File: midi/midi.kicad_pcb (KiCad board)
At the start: 2 copper layers, 69.8 x 125.1 mm, 50 parts, among them J1 Conn_01x02, J2 SJ-43515TS-SMT-TR, M1 DMG4466SSS-13, U1 ESP32-S3-WROOM-1-n16, U2 LTC1624CS8_TRPBF, U3 MAX98357A, U4 MAX98357A, U5 CD74HC154M96

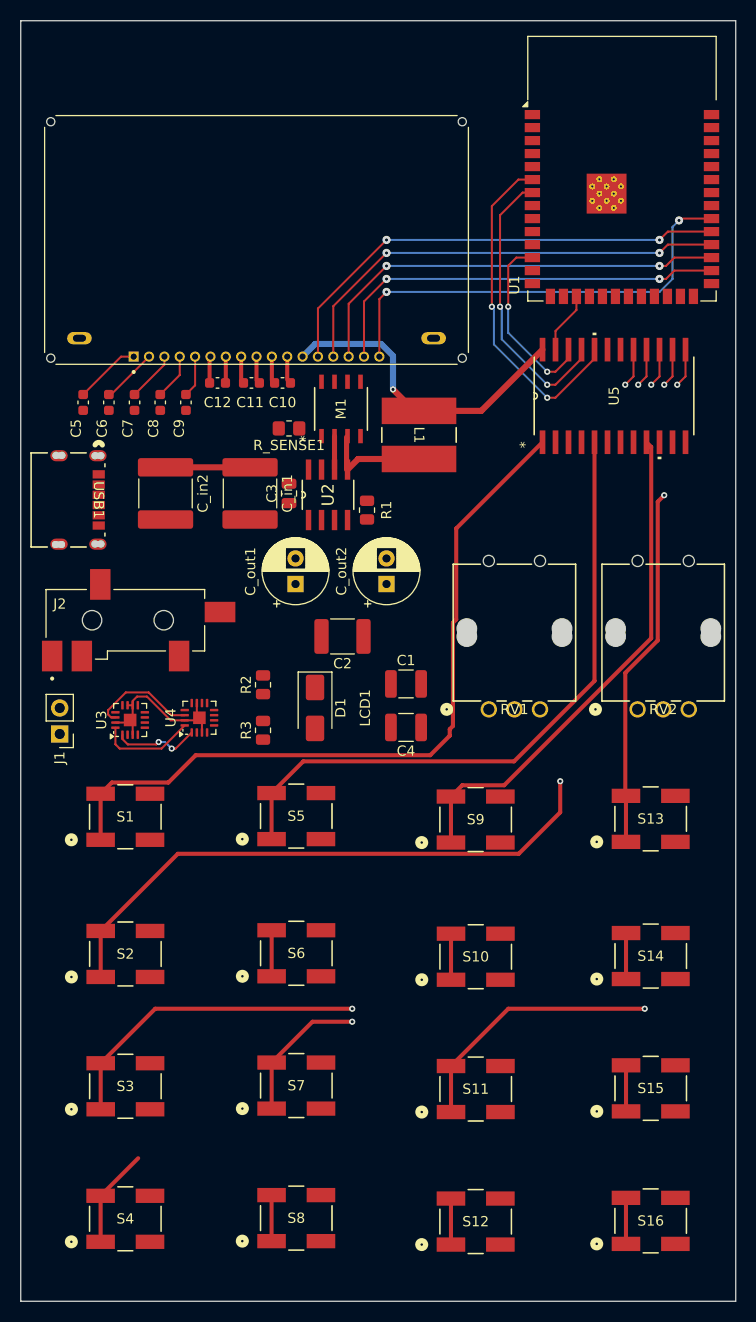
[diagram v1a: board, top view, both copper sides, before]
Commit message: assign more footprints
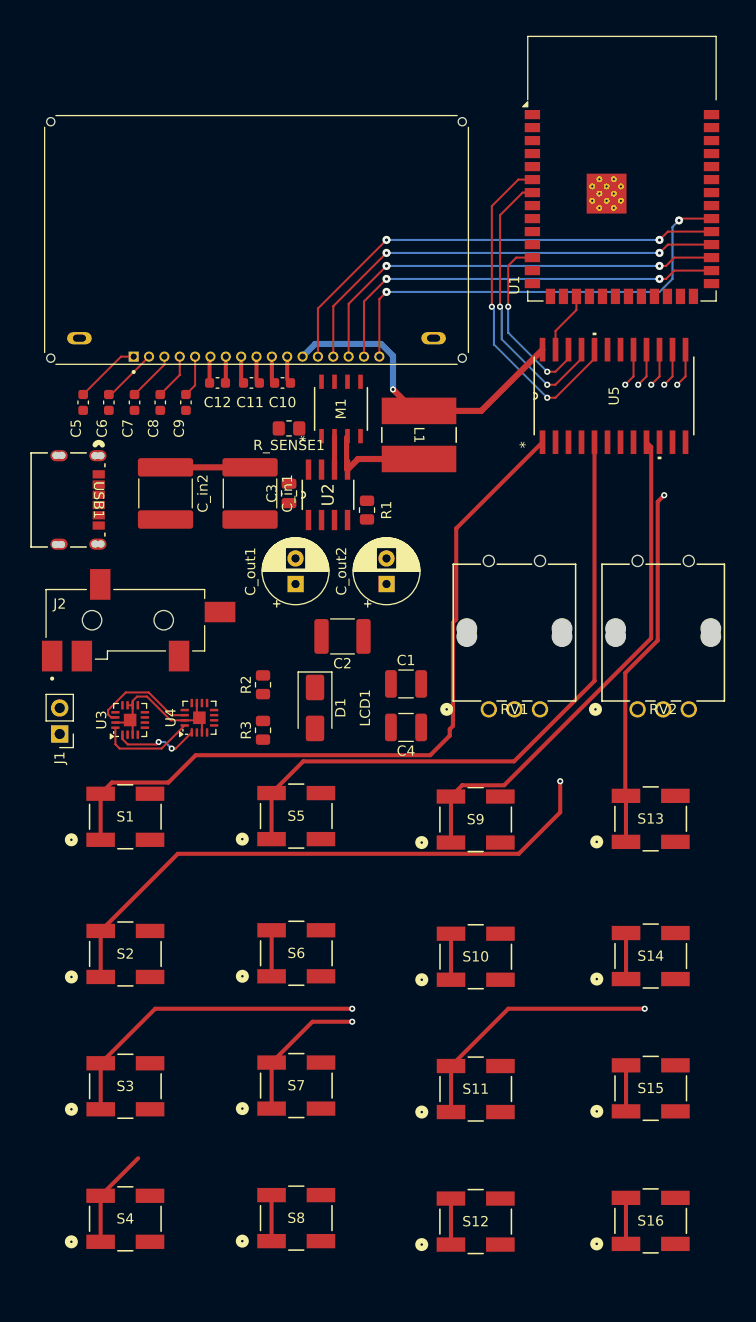
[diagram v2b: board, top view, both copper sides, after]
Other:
- board size 69.8 x 125.1 mm -> 4.4 x 8.7 mm
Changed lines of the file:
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@@
 		)
-	)
-	(gr_line
-		(start 119.38 39.37)
-		(end 119.38 164.465)
-		(stroke
-			(width 0.05)
-			(type default)
-		)
-		(layer "Edge.Cuts")
-	)
-	(gr_line
-		(start 49.53 164.465)
-		(end 49.53 39.37)
-		(stroke
-			(width 0.05)
-			(type default)
-		)
-		(layer "Edge.Cuts")
-	)
-	(gr_line
-		(start 49.53 39.37)
-		(end 119.38 39.37)
-		(stroke
-			(width 0.05)
-			(type default)
-		)
-		(layer "Edge.Cuts")
-	)
-	(gr_line
-		(start 119.38 164.465)
-		(end 49.53 164.465)
-		(stroke
-			(width 0.05)
-			(type default)
-		)
-		(layer "Edge.Cuts")
 	)
 	(segment

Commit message: layout progress
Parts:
- removed C_in1, C_in2: 22µF / 35V, Capacitor_SMD:C_2220_5750Metric
- removed C_out1, C_out2: 100µF / 10V, Capacitor_THT:CP_Radial_D6.3mm_P2.50mm
- removed D1: MBRS340T3, Diode_SMD:D_SMA
- removed M1: DMG4466SSS-13, DMG4466SSS_13:SO-8_DIO
- removed R_SENSE1: 0.05Ω, Resistor_SMD:R_0805_2012Metric_Pad1.20x1.40mm_HandSolder
- removed S1, S10, S11, S12, S13, S14, S15, S16, S2, S3, S4, S5, S6, S7, S8, S9: KS-01Q-01_Obsolete, BTN_TL3301AF160QJ:TL3301AF160QJ_EWI
- removed USB1: USB4125-GF-A, USB4125_GF_A:CONN6_USB4125_GCT
- added C13: .1µF, Capacitor_SMD:C_0603_1608Metric_Pad1.08x0.95mm_HandSolder, F.Cu at (164.5, 71.8)
- added C14: .1µF, Capacitor_SMD:C_0603_1608Metric_Pad1.08x0.95mm_HandSolder, F.Cu at (164.5, 75.6)
- added J3: USB_C_Receptacle_USB2.0_16P, USB4105-GF-A:GCT_USB4105-GF-A, F.Cu at (213.4, 82.5)
- added R4: 5.1k, Resistor_SMD:R_0805_2012Metric_Pad1.20x1.40mm_HandSolder, F.Cu at (210.2, 92.7)
- added R5: 5.1k, Resistor_SMD:R_0805_2012Metric_Pad1.20x1.40mm_HandSolder, F.Cu at (210.2, 97.2)
- added SW1: Reset, Button_Switch_THT:SW_PUSH_6mm_H5mm, F.Cu at (176.0, 69.6)
- added SW10: SW_Push, Button_Switch_THT:SW_PUSH_6mm_H5mm, F.Cu at (208.2, 150.2)
- added SW11: SW_Push, Button_Switch_THT:SW_PUSH_6mm_H5mm, F.Cu at (152.4, 104.4)
- added SW12: SW_Push, Button_Switch_THT:SW_PUSH_6mm_H5mm, F.Cu at (152.4, 119.0)
- added SW13: SW_Push, Button_Switch_THT:SW_PUSH_6mm_H5mm, F.Cu at (170.7, 104.5)
- added SW14: SW_Push, Button_Switch_THT:SW_PUSH_6mm_H5mm, F.Cu at (189.8, 104.5)
- added SW15: SW_Push, Button_Switch_THT:SW_PUSH_6mm_H5mm, F.Cu at (208.1, 104.5)
- added SW16: SW_Push, Button_Switch_THT:SW_PUSH_6mm_H5mm, F.Cu at (170.7, 119.0)
- added SW17: SW_Push, Button_Switch_THT:SW_PUSH_6mm_H5mm, F.Cu at (189.8, 119.0)
- added SW18: SW_Push, Button_Switch_THT:SW_PUSH_6mm_H5mm, F.Cu at (208.2, 119.0)
- added SW2: Boot, Button_Switch_THT:SW_PUSH_6mm_H5mm, F.Cu at (151.8, 65.4)
- added SW3: SW_Push, Button_Switch_THT:SW_PUSH_6mm_H5mm, F.Cu at (152.4, 134.3)
- added SW4: SW_Push, Button_Switch_THT:SW_PUSH_6mm_H5mm, F.Cu at (170.7, 134.3)
- added SW5: SW_Push, Button_Switch_THT:SW_PUSH_6mm_H5mm, F.Cu at (189.8, 134.3)
- added SW6: SW_Push, Button_Switch_THT:SW_PUSH_6mm_H5mm, F.Cu at (208.2, 134.3)
- added SW7: SW_Push, Button_Switch_THT:SW_PUSH_6mm_H5mm, F.Cu at (152.4, 149.9)
- added SW8: SW_Push, Button_Switch_THT:SW_PUSH_6mm_H5mm, F.Cu at (170.7, 150.2)
- added SW9: SW_Push, Button_Switch_THT:SW_PUSH_6mm_H5mm, F.Cu at (189.7, 150.2)
- C1: value 100pF -> 22µF; footprint Capacitor_SMD:C_1210_3225Metric -> Capacitor_SMD:C_0603_1608Metric_Pad1.08x0.95mm_HandSolder
- C2: value 470pF -> 10µF; footprint Capacitor_SMD:C_1812_4532Metric -> Capacitor_SMD:C_0603_1608Metric_Pad1.08x0.95mm_HandSolder
- C3: value 1000pF -> .1µF; footprint Capacitor_SMD:C_0805_2012Metric -> Capacitor_SMD:C_0603_1608Metric_Pad1.08x0.95mm_HandSolder
- C4: value 0.1µ -> 1µF; footprint Capacitor_SMD:C_1210_3225Metric -> Capacitor_SMD:C_0603_1608Metric_Pad1.08x0.95mm_HandSolder
- L1: value 10µH -> 1µH; footprint SRR6038_100Y:IND_BOURNS_SRR6038 -> Inductor_SMD:L_0805_2012Metric_Pad1.15x1.40mm_HandSolder
- R1: value 6.8k -> 634k; footprint Resistor_SMD:R_0805_2012Metric -> Resistor_SMD:R_0603_1608Metric_Pad0.98x0.95mm_HandSolder
- R2: value 35.7k -> 634k; footprint Resistor_SMD:R_0805_2012Metric -> Resistor_SMD:R_0603_1608Metric_Pad0.98x0.95mm_HandSolder
- R3: value 20k -> 10k; footprint Resistor_SMD:R_0805_2012Metric -> Resistor_SMD:R_0603_1608Metric_Pad0.98x0.95mm_HandSolder
- U1: value ESP32-S3-WROOM-1-n16 -> ESP32-S2-SOLO; footprint RF_Module:ESP32-S3-WROOM-1 -> PCM_Espressif:ESP32-S2-SOLO
- U2: value LTC1624CS8_TRPBF -> SC189ZSKTRT; footprint LTC1624CS8_TRPBF:SOIC127P600X175-8N -> SC189ZSKTRT:SOT23-5-SC189_SEM
- moved J2 165.8 mm to (214.7, 67.0), turned to 180 degrees
- moved J1 154.0 mm to (204.5, 79.4), turned to 0 degrees
- moved C2 133.4 mm to (214.0, 89.9), turned to -90 degrees
- moved R3 132.4 mm to (204.5, 91.4), turned to 180 degrees
- moved U4 131.2 mm to (192.9, 70.5), turned to 0 degrees
- moved U3 129.1 mm to (183.8, 70.5), turned to 0 degrees
- moved C10 126.2 mm to (200.7, 61.6)
- moved U2 125.7 mm to (204.8, 96.5)
- moved C11 125.5 mm to (196.8, 61.6)
- moved C12 125.1 mm to (193.2, 61.6)
- moved C6 125.0 mm to (182.3, 62.2)
- moved C9 125.0 mm to (189.9, 62.2)
- moved C5 125.0 mm to (179.8, 62.2)
- moved C7 125.0 mm to (184.8, 62.2)
- moved C8 125.0 mm to (187.4, 62.2)
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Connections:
- C1 pad 1: Net-(U2-VFB) -> +3V3
- C1 pad 2: Net-(U2-GND) -> GND
- C2 pad 1: Net-(C2-Pad1) -> +5V
- C2 pad 2: Net-(U2-ITH/RUN) -> GND
- C3 pad 1: Net-(U2-SENSE-) -> GND
- C3 pad 2: /5V -> Net-(U1-EN)
- C4 pad 1: Net-(U2-BOOST) -> GND
- C4 pad 2: Net-(D1-K) -> +3V3
- L1 pad 1: Net-(D1-K) -> Net-(U2-LX)
- L1 pad 2: /3V3 -> +3V3
- LCD1 pad 12: /3V3 -> +3V3
- R1 pad 1: Net-(U2-GND) -> +3V3
- R1 pad 2: Net-(C2-Pad1) -> Net-(U3-~{SD_MODE})
- R2 pad 1: Net-(U2-VFB) -> +3V3
- R2 pad 2: /3V3 -> Net-(U4-~{SD_MODE})
- R3 pad 1: GND -> +3V3
- R3 pad 2: Net-(U2-VFB) -> Net-(U1-EN)
- U1 pad 11: unconnected-(U1-IO18-Pad11) -> /AUDIO.BCLK
- U1 pad 12: /BTND1 -> unconnected-(U1-GPIO8/TOUCH8/ADC1_CH7-Pad12)
- U1 pad 13: unconnected-(U1-IO19-Pad13) -> /USB.D-
- U1 pad 14: unconnected-(U1-IO20-Pad14) -> /USB.D+
- U1 pad 15: unconnected-(U1-IO3-Pad15) -> /AUDIO.DIN
- U1 pad 16: /AUDIO.DIN -> unconnected-(U1-GPIO46-Pad16)
- U1 pad 17: /BTND0 -> unconnected-(U1-GPIO9/TOUCH9/ADC1_CH8/FSPIHD-Pad17)
- U1 pad 2: /3V3 -> +3V3
- U1 pad 23: unconnected-(U1-IO21-Pad23) -> /LCD.RST
- U1 pad 24: /AUDIO.BCLK -> unconnected-(U1-SPIIO4/GPIO33/FSPIHD-Pad24)
- U1 pad 25: /AUDIO.LRCLK -> /LCD.CS1
- U1 pad 26: /S18 -> /LCD.A0
- U1 pad 27: unconnected-(U1-IO0-Pad27) -> Net-(U1-GPIO0)
- U1 pad 28: /LCD.RST -> /LCD.SI
- U1 pad 29: /LCD.A0 -> /LCD.SCL
- U1 pad 3: /EN-ESP32 -> Net-(U1-EN)
- U1 pad 30: /LCD.SCL -> unconnected-(U1-SPIDQS/GPIO37/FSPIQ-Pad30)
- U1 pad 31: /LCD.SI -> unconnected-(U1-GPIO38/FSPIWP-Pad31)
- U1 pad 32: /LCD.CS1 -> /BTND0
- U1 pad 33: unconnected-(U1-IO40-Pad33) -> /BTND1
- U1 pad 34: unconnected-(U1-IO41-Pad34) -> /BTND2
- U1 pad 35: /S17 -> /BTND3
- U1 pad 38: unconnected-(U1-IO2-Pad38) -> /RV2
- U1 pad 39: unconnected-(U1-IO1-Pad39) -> /RV1
- U1 pad 4: /RV1 -> /AUDIO.LRCLK
- U1 pad 5: /RV2 -> unconnected-(U1-GPIO5/TOUCH5/ADC1_CH4-Pad5)
- U1 pad 6: /BTND3 -> unconnected-(U1-GPIO6/TOUCH6/ADC1_CH5-Pad6)
- U1 pad 7: /BTND2 -> unconnected-(U1-GPIO7/TOUCH7/ADC1_CH6-Pad7)
- U2 pad 1: Net-(U2-SENSE-) -> +5V
- U2 pad 2: Net-(U2-ITH/RUN) -> GND
- U2 pad 3: Net-(U2-VFB) -> +5V
- U2 pad 4: Net-(U2-GND) -> +3V3
- U2 pad 5: Net-(D1-K) -> Net-(U2-LX)
- U3 pad 2: unconnected-(U3-GAIN_SLOT-Pad2) -> +3V3
- U3 pad 4: unconnected-(U3-~{SD_MODE}-Pad4) -> Net-(U3-~{SD_MODE})
- U3 pad 7: /3V3 -> +3V3
- U3 pad 8: /3V3 -> +3V3
- U4 pad 2: unconnected-(U4-GAIN_SLOT-Pad2) -> +3V3
- U4 pad 4: unconnected-(U4-~{SD_MODE}-Pad4) -> Net-(U4-~{SD_MODE})
- U4 pad 7: /3V3 -> +3V3
- U4 pad 8: /3V3 -> +3V3
- U5 pad 24: /3V3 -> +3V3
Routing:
- net +3V3: track 0.00 -> 151.2 mm, vias 0 -> 7
- net /RV2: track 0.00 -> 118.3 mm
- net /RV1: track 0.00 -> 94.6 mm
- net Net-(U1-EN): track 0.00 -> 89.9 mm, vias 0 -> 2
- net /USB.D-: track 0.00 -> 74.8 mm, vias 0 -> 2
- net /USB.D+: track 0.00 -> 72.9 mm, vias 0 -> 2
- net /S6: track 4.50 -> 76.4 mm, vias 0 -> 1
- net /S8: track 4.50 -> 70.9 mm, vias 0 -> 1
- net /S4: track 9.69 -> 74.9 mm, vias 0 -> 3
- net /S7: track 14.0 -> 68.8 mm, vias 1 -> 3
- net /S10: track 4.50 -> 57.7 mm, vias 0 -> 3
- net /AUDIO.LRCLK: track 10.4 -> 58.2 mm, vias 0 -> 3
- net /S15: track 8.26 -> 54.7 mm, vias 1 -> 2
- net /AUDIO.BCLK: track 9.50 -> 54.0 mm, vias 0 -> 3
- net /S14: track 8.26 -> 51.7 mm, vias 1 -> 2
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- added copper zone on B.Cu, net GND
- added copper zone on F.Cu, net GND
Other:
- board size 4.4 x 8.7 mm -> 73 x 129.5 mm

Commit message: fix some layout issues
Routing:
- net Net-(U1-GPIO0): track 24.4 -> 37.4 mm
- net GND: track 17.1 -> 28.3 mm, vias 2 -> 4
- net Net-(U1-EN): track 89.9 -> 94.8 mm
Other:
- board size 73 x 129.5 mm -> 74.9 x 129.5 mm

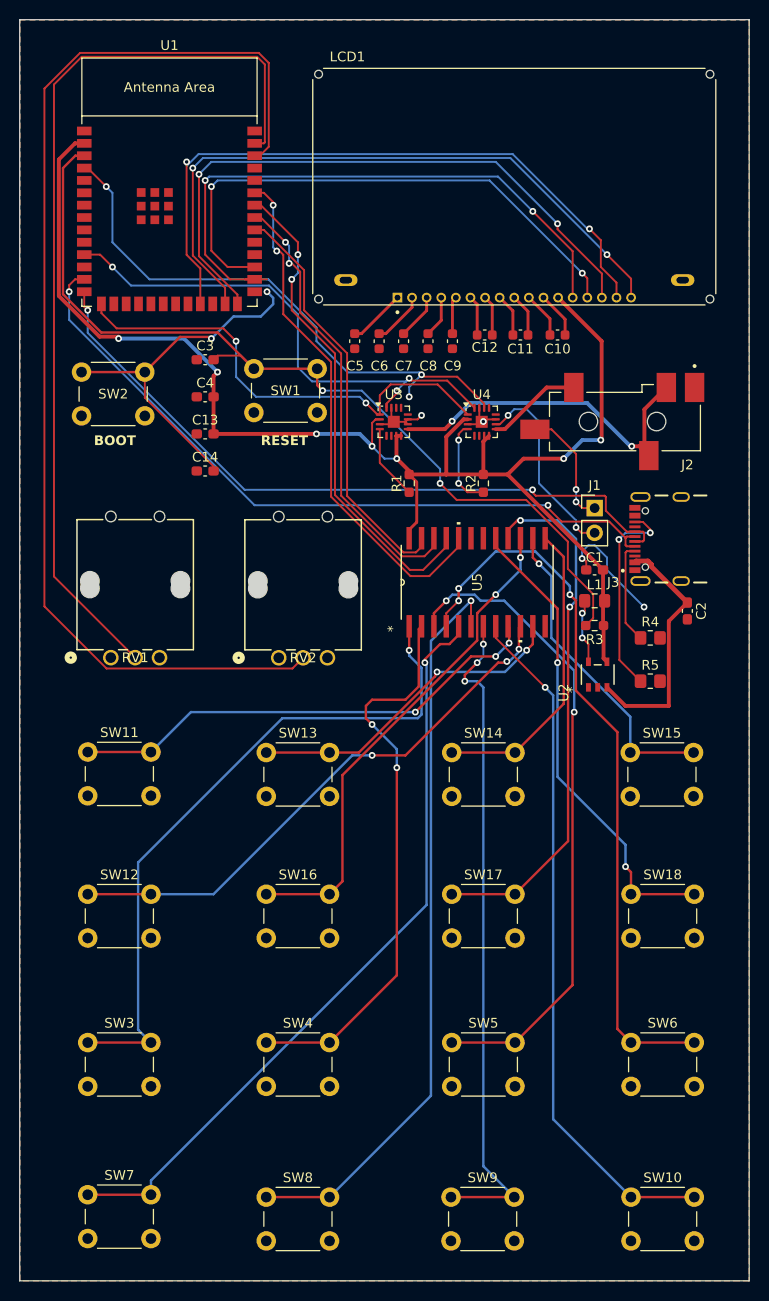
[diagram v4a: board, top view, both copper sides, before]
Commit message: fixed ~60 clearance errors around LCD area
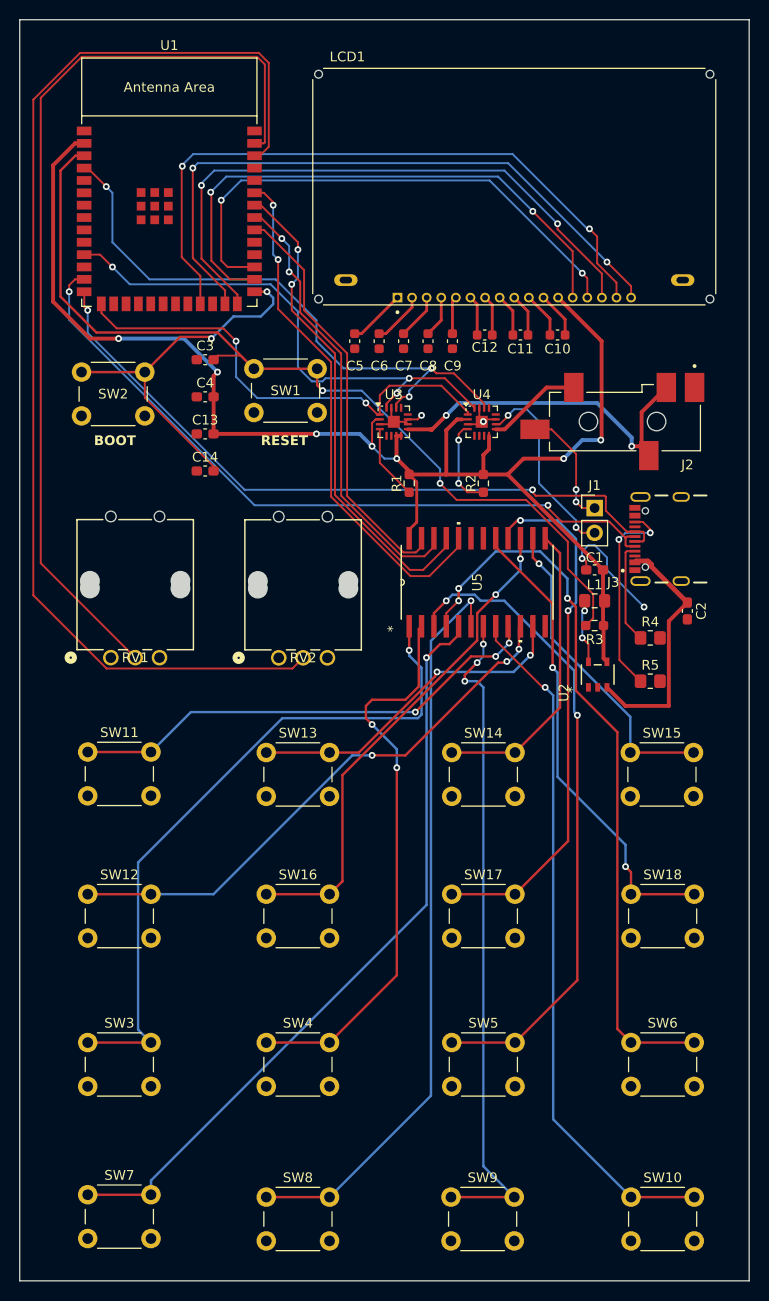
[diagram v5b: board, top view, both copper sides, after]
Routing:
- net /LCD.SI: track 61.8 -> 58.1 mm
- net /AUDIO.LRCLK: track 58.2 -> 61.7 mm
- net /LCD.SCL: track 56.8 -> 54.5 mm
- net /LCD.A0: track 64.4 -> 62.8 mm
- net Net-(U1-GPIO0): track 37.4 -> 38.7 mm
- net /RV1: track 94.6 -> 95.7 mm
- net +3V3: track 151.2 -> 152.3 mm
- net /RV2: track 118.3 -> 119.2 mm
- net /LCD.CS1: track 67.8 -> 67.0 mm
- net Net-(U3-OUTP): track 36.3 -> 37.1 mm
- net /S11: track 34.0 -> 34.5 mm
- net Net-(U1-EN): track 94.8 -> 95.3 mm
- removed copper zone on B.Cu, net GND
- removed copper zone on F.Cu, net GND

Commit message: more DRC fixes
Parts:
- moved J3 4.20 mm to (217.6, 82.5)
- moved R4 3.42 mm to (213.4, 94.0)
- moved R5 3.42 mm to (213.4, 98.4)
- moved J2 3.35 mm to (218.1, 67.0)
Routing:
- net /3V3: track 0.00 -> 26.1 mm, vias 0 -> 2
- net +3V3: track 152.3 -> 163.3 mm
- net +5V: track 25.9 -> 20.3 mm
- net /USB.D-: track 74.8 -> 80.3 mm
- net /RV2: track 119.2 -> 124.5 mm
- net /RV1: track 95.7 -> 100.7 mm
- net Net-(J3-CC2): track 21.3 -> 25.8 mm, vias 2 -> 0
- net Net-(U4-OUTP): track 9.81 -> 13.2 mm
- net /S1: track 70.5 -> 67.3 mm
- net Net-(J3-CC1): track 10.4 -> 13.6 mm
- net /S14: track 51.7 -> 54.8 mm, vias 2 -> 6
- net /USB.D+: track 72.9 -> 75.9 mm
- net GND: track 28.3 -> 31.2 mm, vias 4 -> 3
- net Net-(U3-OUTP): track 37.1 -> 39.7 mm
- net Net-(J1-Pin_1): track 12.4 -> 9.99 mm
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
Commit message: add mounting holes, slight fixes, redo pours
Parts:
- added H1: MountingHole, MountingHole:MountingHole_2.2mm_M2, F.Cu at (69.8, 39.4)
- added H2: MountingHole, MountingHole:MountingHole_2.2mm_M2, F.Cu at (134.0, 39.4)
- added H3: MountingHole, MountingHole:MountingHole_2.2mm_M2, F.Cu at (69.8, 171.4)
- added H4: MountingHole, MountingHole:MountingHole_2.2mm_M2, F.Cu at (134.0, 171.4)
- moved R4 81.4 mm to (132.6, 104.4)
- moved R5 81.4 mm to (132.6, 108.8)
- moved C12 81.4 mm to (112.5, 72.0)
- moved C6 81.4 mm to (101.6, 72.6)
- moved C9 81.4 mm to (109.1, 72.6)
- moved RV2 81.4 mm to (91.3, 105.1)
- moved SW10 81.4 mm to (127.5, 160.5)
- moved SW13 81.4 mm to (90.0, 114.9)
- moved SW16 81.4 mm to (90.0, 129.4)
- moved SW18 81.4 mm to (127.5, 129.4)
- moved SW4 81.4 mm to (90.0, 144.7)
- moved SW6 81.4 mm to (127.5, 144.7)
- moved SW8 81.4 mm to (90.0, 160.5)
- moved U1 81.4 mm to (80.1, 59.3)
- moved C1 81.4 mm to (123.8, 96.1)
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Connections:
- J2 pad 1: GND -> Net-(U3-OUTN)
- U3 pad 10: GND -> Net-(U3-OUTN)
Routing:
- net Net-(U3-OUTN): track 0.00 -> 38.8 mm, vias 0 -> 2
- net /RV2: track 124.5 -> 94.6 mm, vias 0 -> 2
- net /RV1: track 100.7 -> 73.5 mm, vias 0 -> 2
- net /LCD.RST: track 68.9 -> 82.1 mm
- net Net-(U1-GPIO0): track 38.7 -> 45.5 mm
- net /LCD.CS1: track 67.0 -> 72.3 mm
- net /LCD.SCL: track 54.5 -> 50.8 mm
- net +5V: track 20.3 -> 23.8 mm
- net /BTND3: track 53.6 -> 56.6 mm
- net /BTND2: track 50.6 -> 52.7 mm
- net /LCD.SI: track 58.1 -> 56.4 mm
- net /LCD.A0: track 62.8 -> 64.1 mm
- net /BTND1: track 46.1 -> 47.0 mm
- added copper zone on B.Cu, net GND
- added copper zone on F.Cu, net GND
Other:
- board size 74.9 x 129.5 mm -> 75.6 x 142.2 mm

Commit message: close to finished
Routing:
- net Net-(J3-CC2): track 25.8 -> 23.5 mm
- net /BTND3: track 56.6 -> 55.5 mm
- net /BTND2: track 52.7 -> 51.9 mm
- net Net-(U1-GPIO0): track 45.5 -> 45.0 mm
